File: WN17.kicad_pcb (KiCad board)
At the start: 2 copper layers, 41 x 41 mm, 4 parts, among them J1 Conn_01x02_Pin, U1 AS5600, U2 DRV8434APWPR

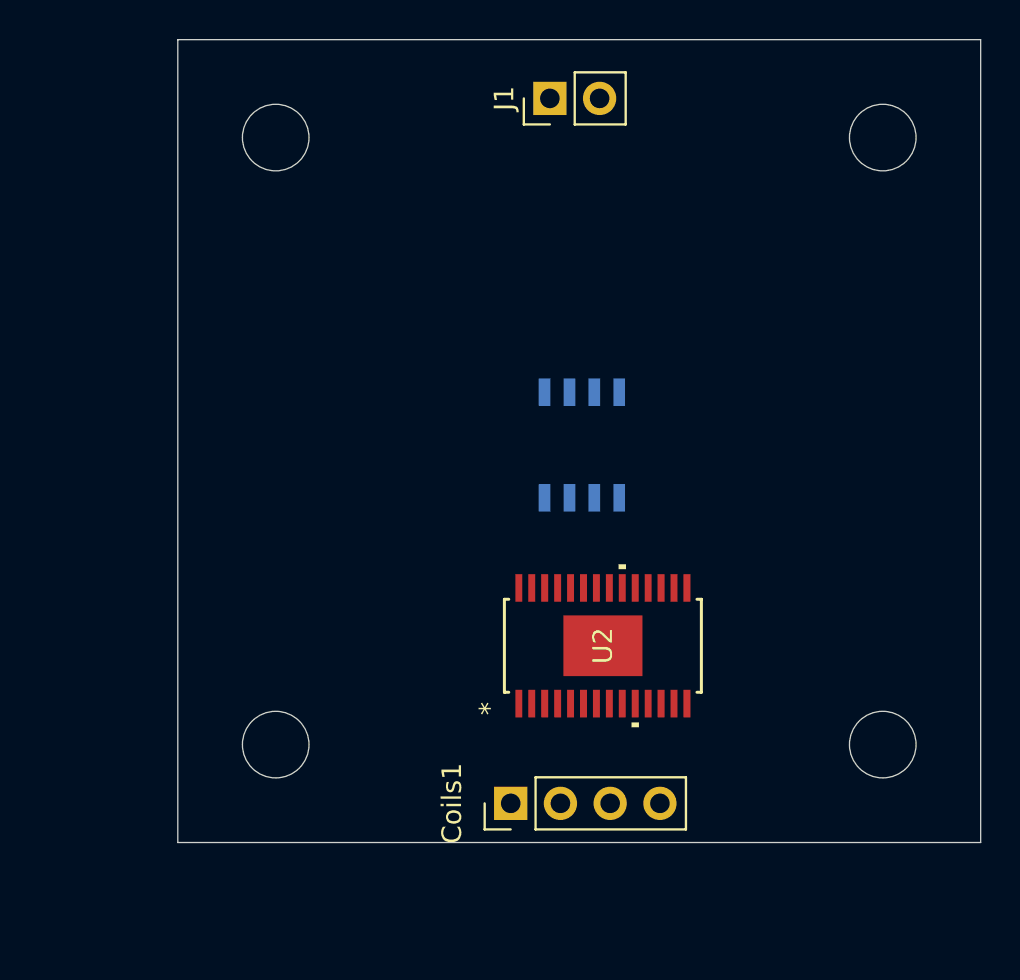
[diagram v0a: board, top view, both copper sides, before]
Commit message: Added Motor driver capacitors and  supply
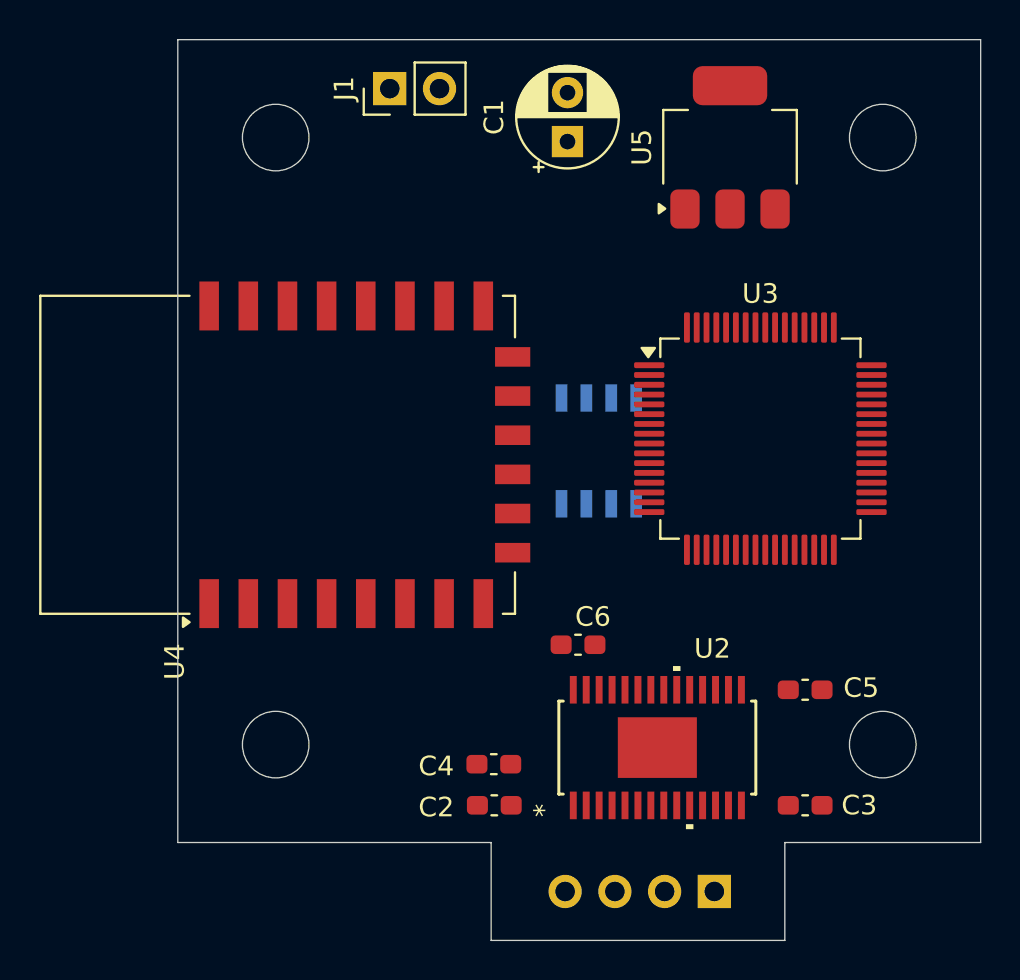
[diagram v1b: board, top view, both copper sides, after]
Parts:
- added C1: 10uF, Capacitor_THT:CP_Radial_D5.0mm_P2.50mm, F.Cu at (114.9, 60.2)
- added C2: 0.01uF, Capacitor_SMD:C_0603_1608Metric_Pad1.08x0.95mm_HandSolder, F.Cu at (111.2, 94.1)
- added C3: 0.01uF, Capacitor_SMD:C_0603_1608Metric_Pad1.08x0.95mm_HandSolder, F.Cu at (127.0, 94.1)
- added C4: 0.22uF, Capacitor_SMD:C_0603_1608Metric_Pad1.08x0.95mm_HandSolder, F.Cu at (111.1, 92.0)
- added C5: 0.47uF, Capacitor_SMD:C_0603_1608Metric_Pad1.08x0.95mm_HandSolder, F.Cu at (127.0, 88.2)
- added C6: 0.47uF, Capacitor_SMD:C_0603_1608Metric_Pad1.08x0.95mm_HandSolder, F.Cu at (115.4, 85.9)
- added U3: STM32L476RGTx, Package_QFP:LQFP-64_10x10mm_P0.5mm, F.Cu at (124.8, 75.4)
- added U4: ESP-12F, RF_Module:ESP-12E, F.Cu at (100.1, 76.2)
- added U5: AMS1117, Package_TO_SOT_SMD:SOT-223-3_TabPin2, F.Cu at (123.2, 60.5)
- Coils1: moved to B.Cu
- moved Coils1 11.3 mm to (122.4, 98.5)
- moved J1 8.19 mm to (105.8, 57.5)
- moved U2 5.90 mm to (119.5, 91.2)
- moved U1 0.92 mm to (116.5, 76.0)
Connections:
- U2 pad 1: unconnected-(U2-VCP-Pad1) -> Net-(U2-VCP)
- U2 pad 12: unconnected-(U2-PGND-Pad12) -> GND
- U2 pad 13: unconnected-(U2-VM-Pad13) -> VDD
- U2 pad 14: unconnected-(U2-GND-Pad14) -> GND
- U2 pad 15: unconnected-(U2-DVDD-Pad15) -> Net-(U2-DVDD)
- U2 pad 2: unconnected-(U2-VM-Pad2) -> VDD
- U2 pad 27: unconnected-(U2-CPL-Pad27) -> Net-(U2-CPL)
- U2 pad 28: unconnected-(U2-CPH-Pad28) -> Net-(U2-CPH)
- U2 pad 3: unconnected-(U2-PGND-Pad3) -> GND
- U2 pad EPAD: unconnected-(U2-GND-PadEPAD) -> GND
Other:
- board size 41 x 41 mm -> 41 x 46 mm
